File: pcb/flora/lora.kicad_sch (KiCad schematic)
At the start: 11 parts, among them U1 Ai-Thinker-Ra-01

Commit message: released Rev A
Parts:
- U1: LCSC Ra-01SC -> C2830749
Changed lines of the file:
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@@
       (effects (font (size 1.27 1.27)) hide)
     )
-    (property "LCSC" "Ra-01SC" (id 4) (at 138.43 92.71 0)
+    (property "LCSC" "C2830749" (id 4) (at 138.43 92.71 0)
       (effects (font (size 1.27 1.27)) hide)
     )

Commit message: added image
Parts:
- U1: value Ai-Thinker-Ra-01 -> Ai-Thinker-Ra-01H; symbol RF_JLC:Ai-Thinker-Ra-01 -> RF_JLC:Ai-Thinker-Ra-01H; LCSC C2830749 -> C503593
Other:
- title: (none) -> FLORA
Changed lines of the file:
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@@
 (kicad_sch (version 20211123) (generator eeschema)
   (paper "A3")
+  (title_block
+    (title "FLORA")
+    (date "2022-06-01")
+    (rev "B")
+  )
   (junction (at 128.905 57.15) (diameter 0) (color 0 0 0 0)
   )
@@
     (pin "2")
   )
-  (symbol (lib_id "RF_JLC:Ai-Thinker-Ra-01") (at 138.43 92.71 0) (unit 1)
+  (symbol (lib_id "RF_JLC:Ai-Thinker-Ra-01H") (at 138.43 92.71 0) (unit 1)
     (in_bom yes) (on_board yes) (fields_autoplaced)
     (property "Reference" "U1" (id 0) (at 140.4494 76.0435 0)
       (effects (font (size 1.27 1.27)) (justify left))
     )
-    (property "Value" "Ai-Thinker-Ra-01" (id 1) (at 140.4494 78.8186 0)
+    (property "Value" "Ai-Thinker-Ra-01H" (id 1) (at 140.4494 78.8186 0)
       (effects (font (size 1.27 1.27)) (justify left))
     )
@@
       (effects (font (size 1.27 1.27)) hide)
     )
-    (property "Datasheet" "https://docs.ai-thinker.com/_media/lora/docs/ra-01s_specification.pdf" (id 3) (at 140.97 74.93 0)
-      (effects (font (size 1.27 1.27)) hide)
-    )
-    (property "LCSC" "C2830749" (id 4) (at 138.43 92.71 0)
-      (effects (font (size 1.27 1.27)) hide)
-    )
+    (property "Datasheet" "https://cdn.ozdisan.com/ETicaret_Dosya/632831_134737.pdf" (id 3) (at 140.97 74.93 0)
+      (effects (font (size 1.27 1.27)) hide)
+    )
+    (property "LCSC" "C503593" (id 4) (at 138.43 92.71 0)
+      (effects (font (size 1.27 1.27)) hide)
+    )

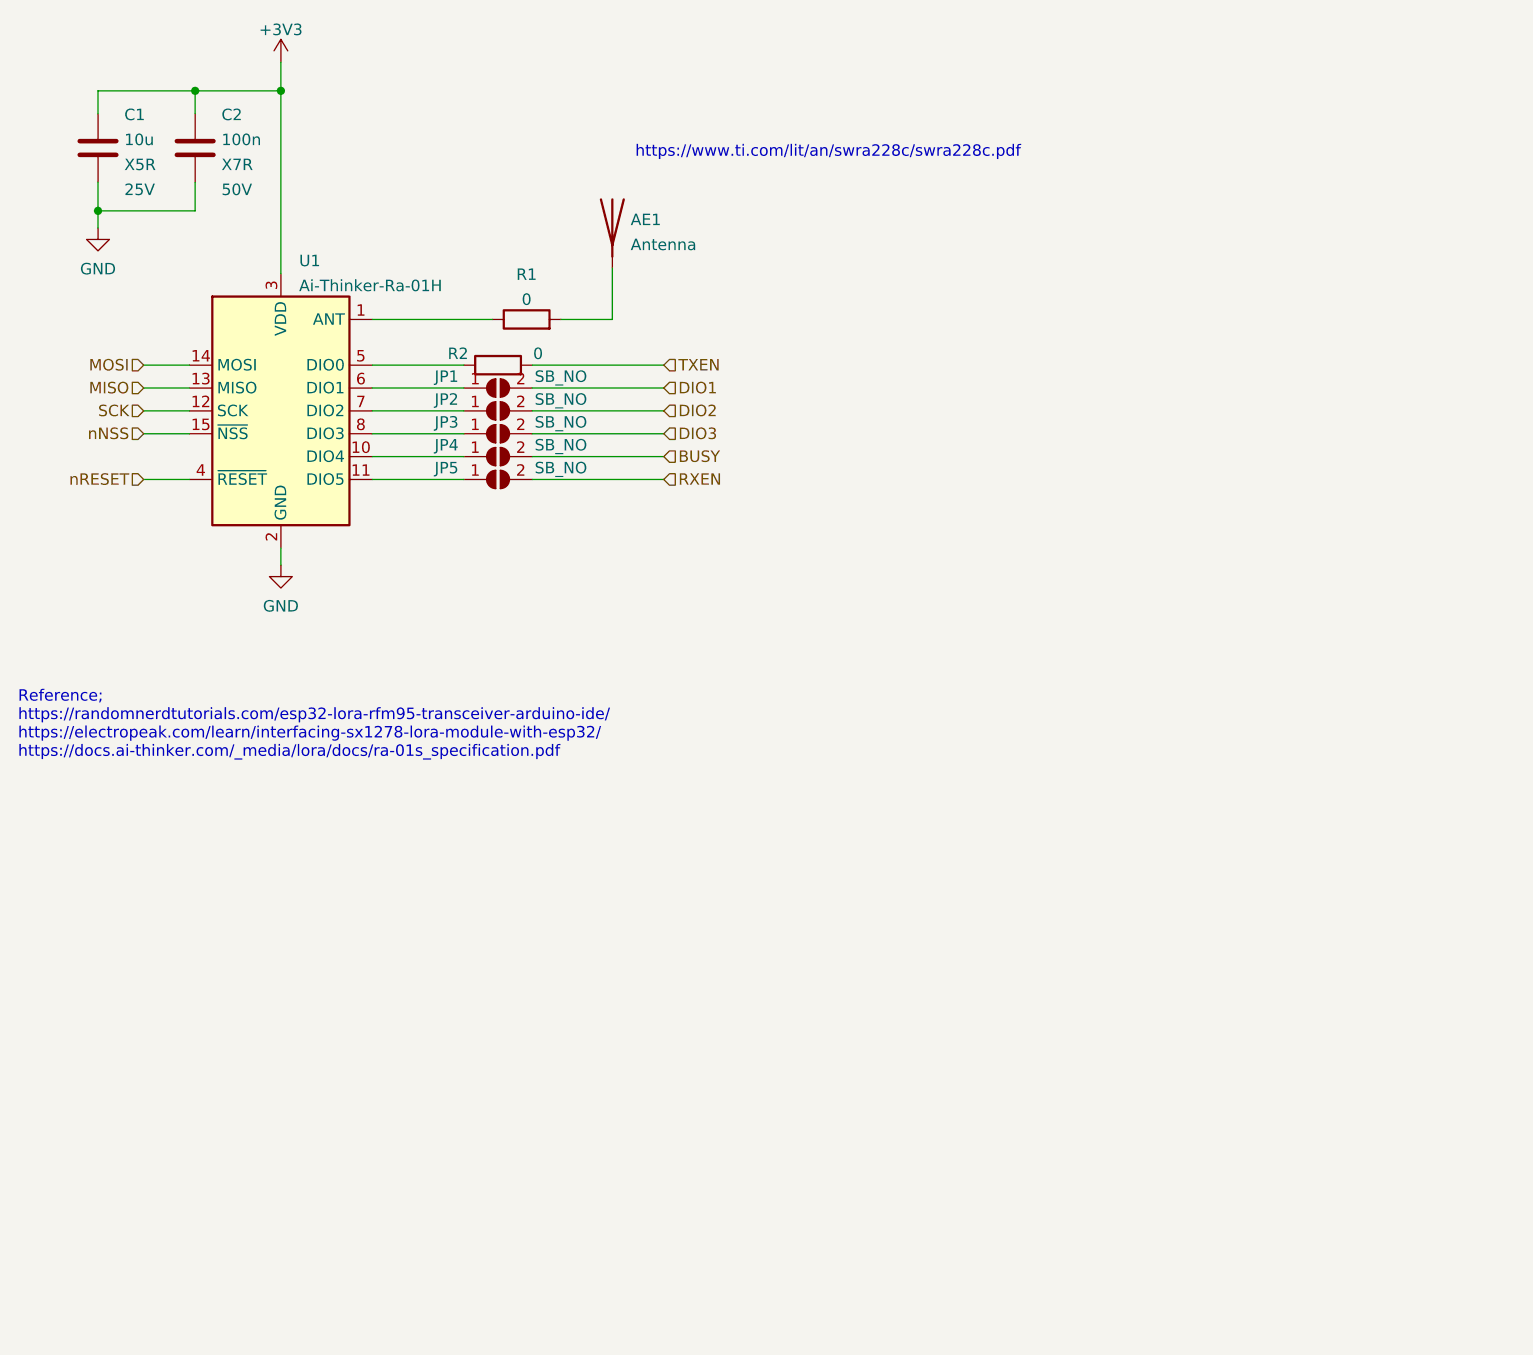
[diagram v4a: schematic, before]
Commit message: Finished schematic for RA-01 design
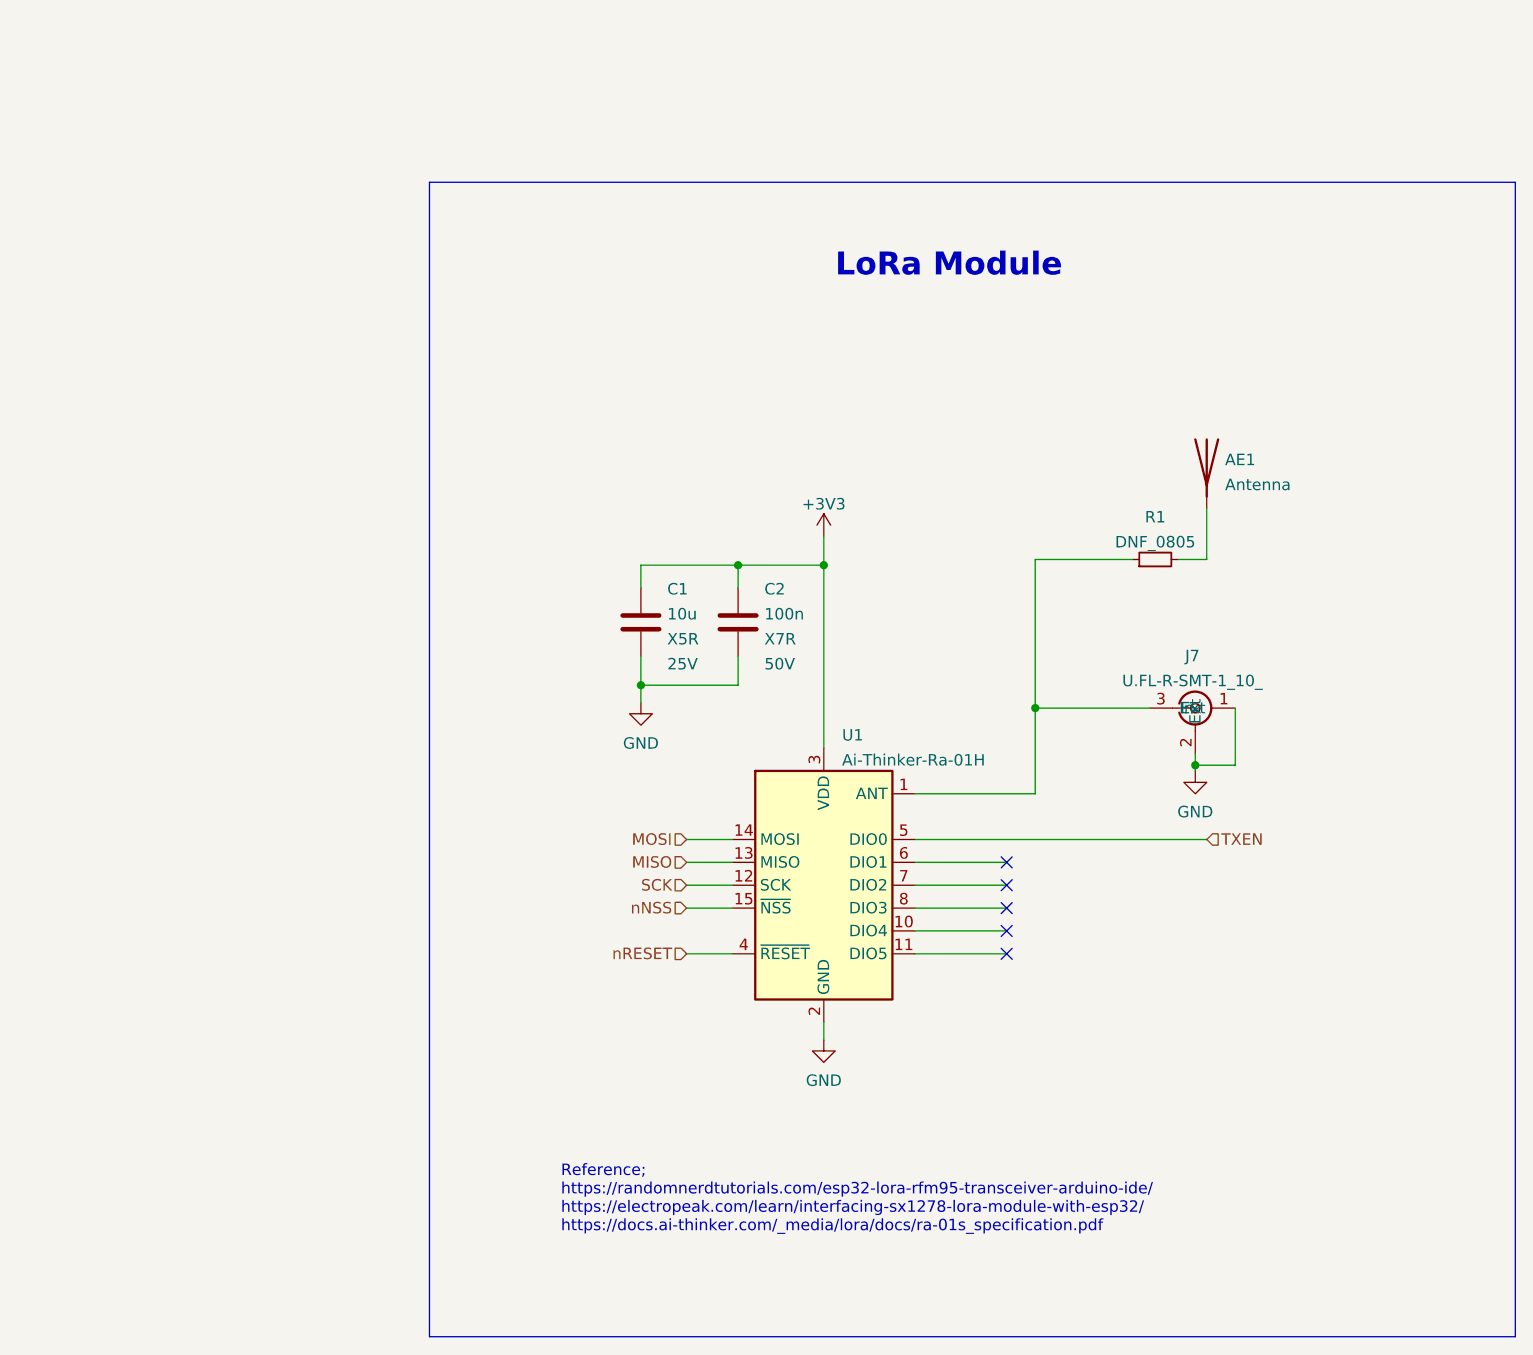
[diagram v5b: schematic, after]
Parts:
- removed JP1, JP2, JP3, JP4, JP5: SB_NO, Jumper:SolderJumper-2_P1.3mm_Open_TrianglePad1.0x1.5mm, symbol personal:SB_NO
- removed R1, R2: 0, Resistor_SMD:R_0805_2012Metric_Pad1.20x1.40mm_HandSolder, symbol Resistor_JLC:0
- added J7: U.FL-R-SMT-1_10_, SamacSys_Parts:U.FL-R-SMT-1_10_, symbol Connector_JLC:U.FL-R-SMT-1_10_
- added R1: DNF_0805, Resistor_SMD:R_0805_2012Metric_Pad1.20x1.40mm_HandSolder, symbol personal:DNF_0805
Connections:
- net GND: now also J7.1 (Ext), J7.2 (Ext)
- net TXEN: now also U1.5 (DIO0)
- net at U1.1 (ANT): now also J7.3 (In), R1.1
- net at AE1.1 (A): now also R1.2
- no-connect marks 0 -> 5
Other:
- note added: "LoRa Module"
- note removed: "https://www.ti.com/lit/an/swra228c/swra228c.pdf"
- title: FLORA -> FLORA-RA01H
- moved on the sheet: AE1, C1, C2, U1
